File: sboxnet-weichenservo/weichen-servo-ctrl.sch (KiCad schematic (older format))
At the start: 2 parts

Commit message: mit weichen-servo-ctrl
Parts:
- added SW5, SW6, SW7, SW8: SW_Push, sboxnet:JTP-1130, symbol Switch:SW_Push
- RN4: renamed from RN?; value R_Network15 -> 4816P-T02-471LF 15x470; footprint (none) -> Package_SO:SOIC-16W_5.3x10.2mm_P1.27mm
- gave numbers to parts that had none: 1
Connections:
- net CTRL_9: now reaches BAR2.1 (A)
- net CTRL_10: now reaches BAR2.2 (A)
- net CTRL_11: now reaches BAR2.3 (A)
- net CTRL_12: now reaches BAR2.4 (A)
- net CTRL_13: now reaches BAR2.5 (A)
- net CTRL_14: now reaches BAR2.6 (A)
- net CTRL_15: now reaches BAR2.7 (A)
- net CTRL_16: now reaches BAR2.8 (A)
- net GND renamed CTRL_1
- net CTRL_1: now also SW5.1, SW6.1, SW7.1, SW8.1
- new net CTRL_2: SW8.2
- new net CTRL_3: SW7.2
- new net CTRL_4: SW6.2
- new net CTRL_5: SW5.2
- no-connect marks 4 -> 11
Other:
- note added: "Aktion"
- note added: "Dn"
- note added: "GND"
- note added: "PD0"
- note added: "PD1"
- note added: "PD2"
- note added: "PD3"
- note added: "PD4"
- note added: "PD5"
- note added: "PD6"
- note added: "PD7"
- note added: "Select"
- note added: "Up"
- moved on the sheet: BAR2, RN4

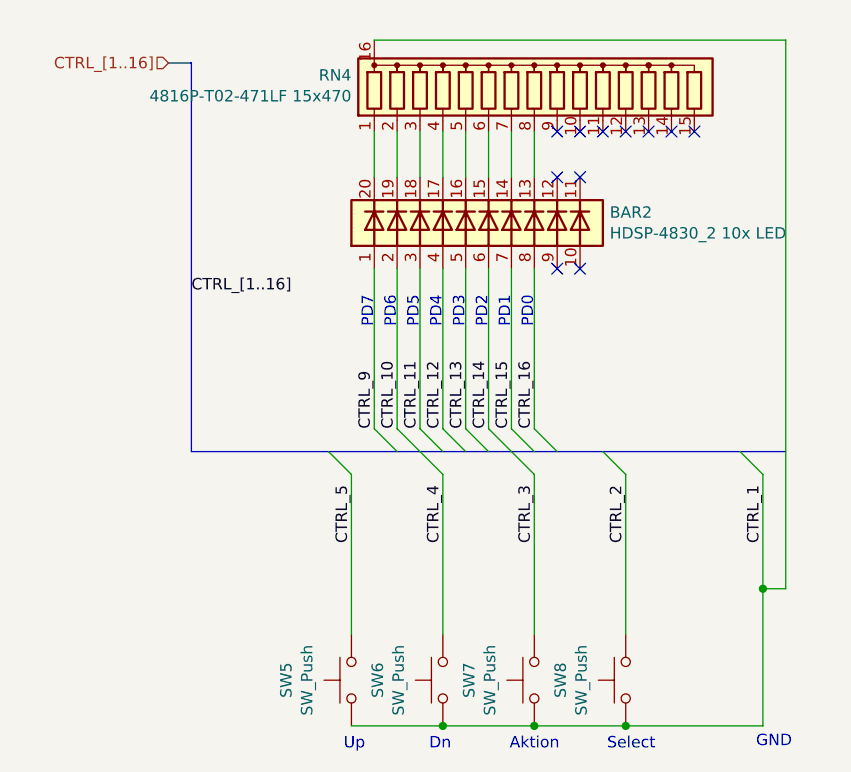
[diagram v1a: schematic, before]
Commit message: weichenservo mit Modulkennung
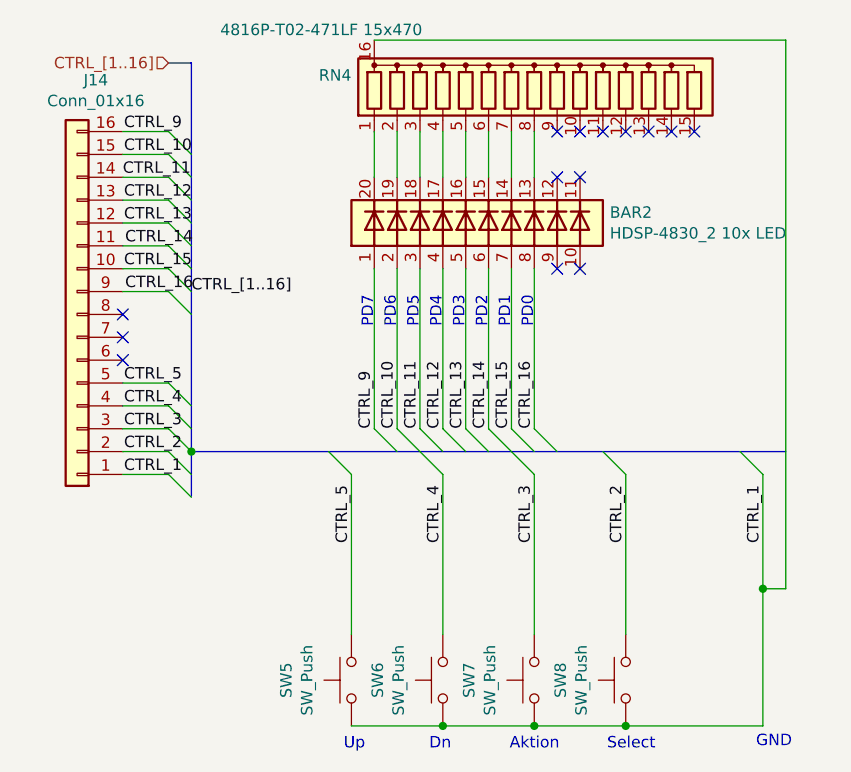
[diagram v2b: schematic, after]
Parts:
- added J14: Conn_01x16, Connector_PinSocket_2.54mm:PinSocket_1x16_P2.54mm_Vertical, symbol Connector_Generic:Conn_01x16
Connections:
- net CTRL_1: now also J14.1 (Pin_1)
- net CTRL_10: now also J14.15 (Pin_15)
- net CTRL_11: now also J14.14 (Pin_14)
- net CTRL_12: now also J14.13 (Pin_13)
- net CTRL_13: now also J14.12 (Pin_12)
- net CTRL_14: now also J14.11 (Pin_11)
- net CTRL_15: now also J14.10 (Pin_10)
- net CTRL_16: now also J14.9 (Pin_9)
- net CTRL_2: now also J14.2 (Pin_2)
- net CTRL_3: now also J14.3 (Pin_3)
- net CTRL_4: now also J14.4 (Pin_4)
- net CTRL_5: now also J14.5 (Pin_5)
- net CTRL_9: now also J14.16 (Pin_16)
- no-connect marks 11 -> 14
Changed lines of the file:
@@
 Wire Bus Line
 	2100 1500 2200 1500
-Wire Bus Line
-	2200 1500 2200 3200
 $Comp
 L LED:HDSP-4830_2 BAR?
@@
 AR Path="/61281C62/6128C339" Ref="RN4"  Part="1"
 F 0 "RN4" H 2900 1646 50  0000 R CNN
-F 1 "4816P-T02-471LF 15x470" H 2900 1555 50  0000 R CNN
+F 1 "4816P-T02-471LF 15x470" H 3210 1845 50  0000 R CNN
 F 2 "Package_SO:SOIC-16W_5.3x10.2mm_P1.27mm" H 3600 1600 50  0001 C CNN
 F 3 "" H 3600 1600 50  0001 C CNN
@@
 Text Notes 3700 2660 1    50   ~ 0
 PD0
+$Comp
+L Connector_Generic:Conn_01x16 J14
+U 1 1 611BEE4E
+P 1700 2600
+F 0 "J14" H 1618 1575 50  0000 C CNN
+F 1 "Conn_01x16" H 1618 1666 50  0000 C CNN
+F 2 "Connector_PinSocket_2.54mm:PinSocket_1x16_P2.54mm_Vertical" H 1700 2600 50  0001 C CNN
+F 3 "~" H 1700 2600 50  0001 C CNN
+	1    1700 2600
+	-1   0    0    1
+$EndComp
+Connection ~ 2200 3200
+Entry Wire Line
+	2100 3300 2200 3400
+Text Label 1905 3300 0    50   ~ 0
+CTRL_1
+Wire Wire Line
+	1900 3300 2100 3300
+Wire Wire Line
+	1900 3200 2100 3200
+Wire Wire Line
+	1900 3100 2100 3100
+Wire Wire Line
+	1900 3000 2100 3000
+Wire Wire Line
+	1900 2900 2100 2900
+Text Label 1905 3200 0    50   ~ 0
+CTRL_2
+Text Label 1905 3100 0    50   ~ 0
+CTRL_3
+Text Label 1905 3000 0    50   ~ 0
+CTRL_4
+Text Label 1905 2900 0    50   ~ 0
+CTRL_5
+Entry Wire Line
+	2100 3200 2200 3300
+Entry Wire Line
+	2100 3100 2200 3200
+Entry Wire Line
+	2100 3000 2200 3100
+Entry Wire Line
+	2100 2900 2200 3000
+NoConn ~ 1900 2800
+NoConn ~ 1900 2700
+NoConn ~ 1900 2600
+Wire Wire Line
+	1900 2500 2100 2500
+Wire Wire Line
+	1900 2400 2100 2400
+Wire Wire Line
+	1900 2300 2100 2300
+Wire Wire Line
+	1900 2200 2100 2200
+Wire Wire Line
+	1900 2100 2100 2100
+Wire Wire Line
+	1900 2000 2100 2000
+Wire Wire Line
+	1900 1900 2100 1900
+Wire Wire Line
+	1900 1800 2100 1800
+Entry Wire Line
+	2100 1800 2200 1900
+Entry Wire Line
+	2100 1900 2200 2000
+Entry Wire Line
+	2100 2000 2200 2100
+Entry Wire Line
+	2100 2100 2200 2200
+Entry Wire Line
+	2100 2200 2200 2300
+Entry Wire Line
+	2100 2300 2200 2400
+Entry Wire Line
+	2100 2400 2200 2500
+Entry Wire Line
+	2100 2500 2200 2600
+Text Label 1905 1800 0    50   ~ 0
+CTRL_9
+Text Label 1905 1900 0    50   ~ 0
+CTRL_10
+Text Label 1900 2000 0    50   ~ 0
+CTRL_11
+Text Label 1905 2100 0    50   ~ 0
+CTRL_12
+Text Label 1905 2200 0    50   ~ 0
+CTRL_13
+Text Label 1910 2300 0    50   ~ 0
+CTRL_14
+Text Label 1905 2400 0    50   ~ 0
+CTRL_15
+Text Label 1910 2500 0    50   ~ 0
+CTRL_16
+Wire Bus Line
+	2200 3200 2200 3395
+Wire Bus Line
+	2200 1500 2200 3200
 Wire Bus Line
 	2200 3200 4800 3200
